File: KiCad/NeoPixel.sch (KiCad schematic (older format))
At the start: 14 parts, among them J701 5V_I/O_1, J702 5V_I/O_2, J703 NEO1, J704 NEO2, J705 NEO3, J706 NEO4, J707 CONN_01X03, U701 TXB0102DCT

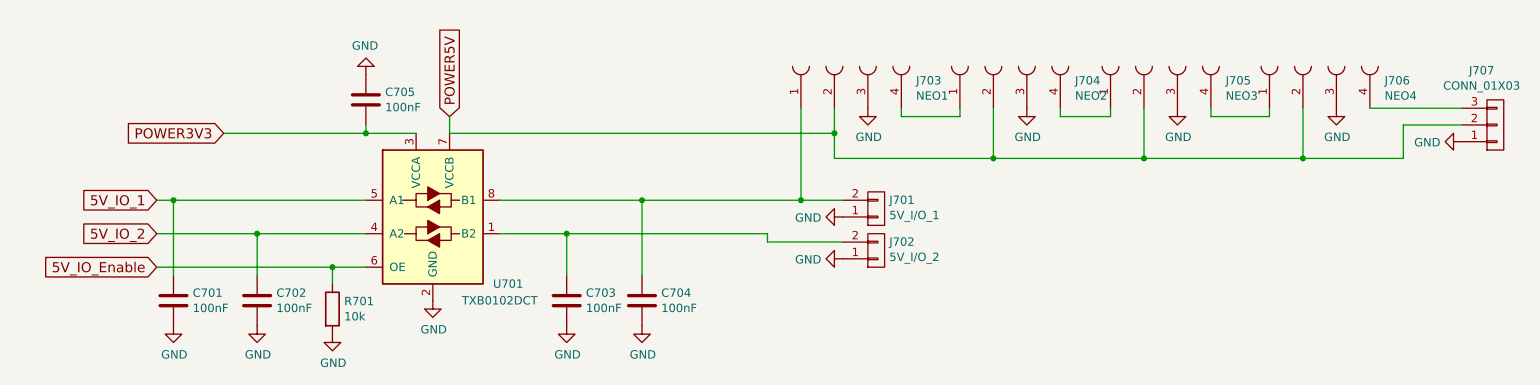
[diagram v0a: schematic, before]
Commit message: Update capacitor values
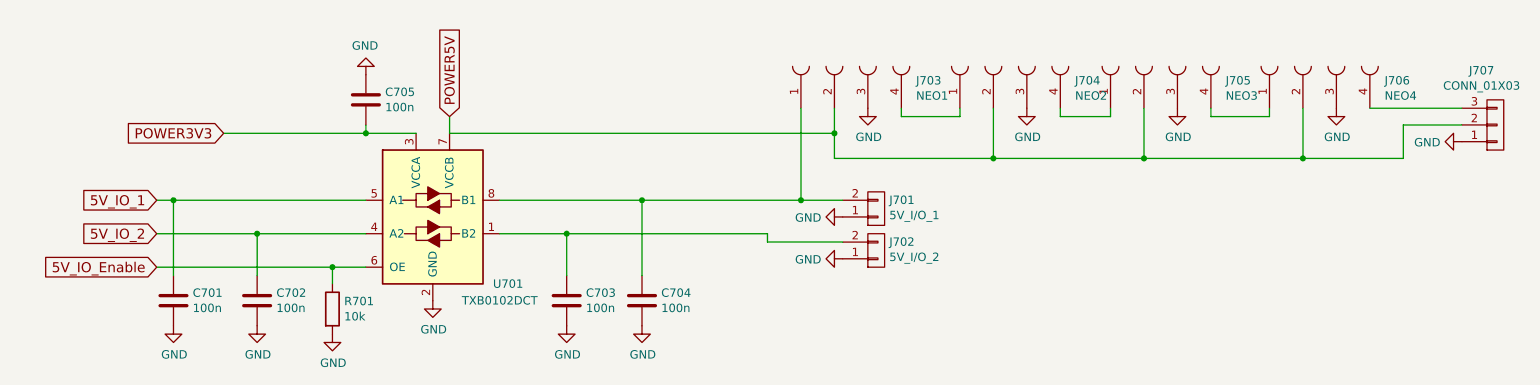
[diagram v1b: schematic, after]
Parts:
- C701, C702, C703, C704, C705: value 100nF -> 100n
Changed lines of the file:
@@
 P 1500 2200
 F 0 "C701" H 1615 2246 50  0000 L CNN
-F 1 "100nF" H 1615 2155 50  0000 L CNN
+F 1 "100n" H 1615 2155 50  0000 L CNN
 F 2 "Capacitors_SMD:C_0805" H 1538 2050 50  0001 C CNN
 F 3 "" H 1500 2200 50  0001 C CNN
@@
 P 2000 2200
 F 0 "C702" H 2115 2246 50  0000 L CNN
-F 1 "100nF" H 2115 2155 50  0000 L CNN
+F 1 "100n" H 2115 2155 50  0000 L CNN
 F 2 "Capacitors_SMD:C_0805" H 2038 2050 50  0001 C CNN
 F 3 "" H 2000 2200 50  0001 C CNN
@@
 P 3850 2200
 F 0 "C703" H 3965 2246 50  0000 L CNN
-F 1 "100nF" H 3965 2155 50  0000 L CNN
+F 1 "100n" H 3965 2155 50  0000 L CNN
 F 2 "Capacitors_SMD:C_0805" H 3888 2050 50  0001 C CNN
 F 3 "" H 3850 2200 50  0001 C CNN
@@
 P 4300 2200
 F 0 "C704" H 4415 2246 50  0000 L CNN
-F 1 "100nF" H 4415 2155 50  0000 L CNN
+F 1 "100n" H 4415 2155 50  0000 L CNN
 F 2 "Capacitors_SMD:C_0805" H 4338 2050 50  0001 C CNN
 F 3 "" H 4300 2200 50  0001 C CNN
@@
 P 2650 1000
 F 0 "C705" H 2765 1046 50  0000 L CNN
-F 1 "100nF" H 2765 955 50  0000 L CNN
+F 1 "100n" H 2765 955 50  0000 L CNN
 F 2 "Capacitors_SMD:C_0805" H 2688 850 50  0001 C CNN
 F 3 "" H 2650 1000 50  0001 C CNN
